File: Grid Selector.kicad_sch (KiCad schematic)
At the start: 74 parts

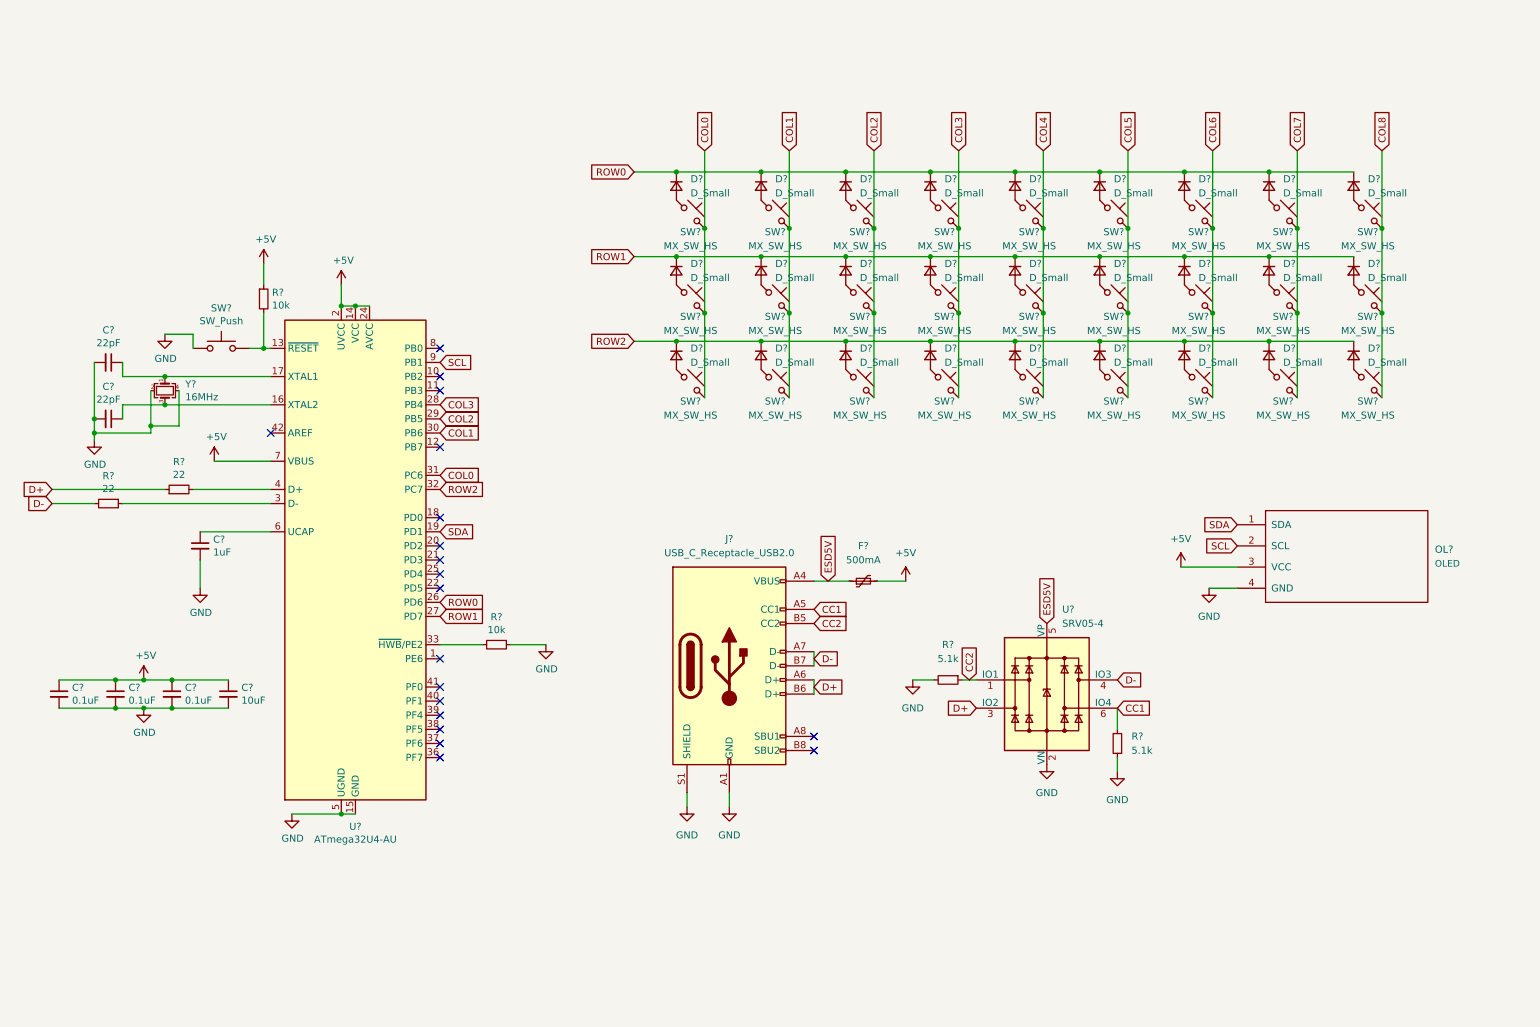
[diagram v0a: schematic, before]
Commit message: added oled library and finished schematics
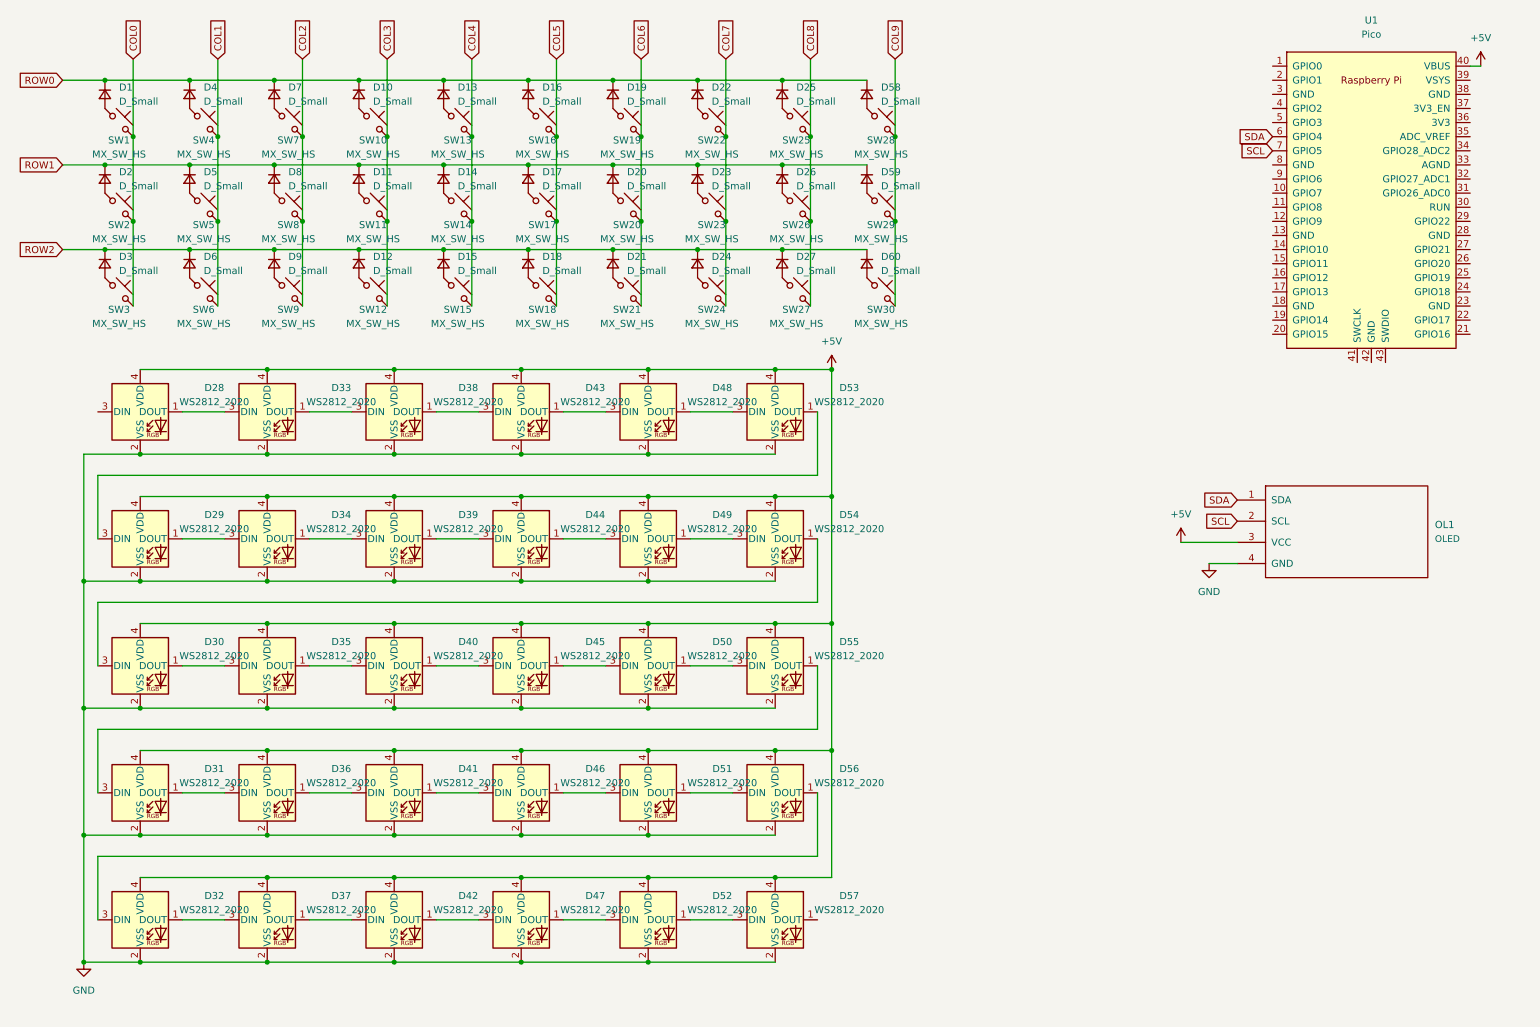
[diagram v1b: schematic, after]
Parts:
- removed C?: 10uF, Capacitor_SMD:C_0805_2012Metric, symbol Device:C_Small
- removed C? (x3): 0.1uF, Capacitor_SMD:C_0805_2012Metric, symbol Device:C_Small
- removed C? (x2): 22pF, Capacitor_SMD:C_0805_2012Metric, symbol Device:C_Small
- removed C?: 1uF, Capacitor_SMD:C_0805_2012Metric, symbol Device:C_Small
- removed F?: 500mA, Fuse:Fuse_1206_3216Metric, symbol Device:Polyfuse_Small
- removed J?: USB_C_Receptacle_USB2.0, Connector_USB:USB_C_Receptacle_HRO_TYPE-C-31-M-12, symbol Connector:USB_C_Receptacle_USB2.0
- removed OL?: OLED, kbd:OLED_v2, symbol kbd:OLED
- removed R? (x2): 5.1k, Resistor_SMD:R_0805_2012Metric, symbol Device:R_Small
- removed R? (x2): 22, Resistor_SMD:R_0805_2012Metric, symbol Device:R_Small
- removed R? (x2): 10k, Resistor_SMD:R_0805_2012Metric, symbol Device:R_Small
- removed SW?: SW_Push, marbastlib-various:SW_SPST_SKQG_WithStem, symbol Switch:SW_Push
- removed U?: ATmega32U4-AU, Package_QFP:TQFP-44_10x10mm_P0.8mm, symbol hayabusa04-rescue:ATmega32U4-AU-MCU_Microchip_ATmega
- removed U?: SRV05-4, Package_TO_SOT_SMD:SOT-23-6, symbol Power_Protection:SRV05-4
- removed Y?: 16MHz, Crystal:Crystal_SMD_3225-4Pin_3.2x2.5mm, symbol Device:Crystal_GND24_Small
- added D28, D29, D30, D31, D32, D33, D34, D35, D36, D37, D38, D39, D40, D41, D42, D43, D44, D45, D46, D47, D48, D49, D50, D51, D52, D53, D54, D55, D56, D57: WS2812_2020, marbastlib-various:LED_WS2812_2020, symbol marbastlib-various:WS2812_2020
- added D58, D59, D60: D_Small, Diode_SMD:D_SOD-123, symbol Device:D_Small
- added OL1: OLED, kbd:OLED_v2, symbol kbd:OLED
- added SW28, SW29, SW30: MX_SW_HS, marbastlib-mx:SW_MX_HS_1u, symbol marbastlib-mx:MX_SW_HS
- added U1: Pico, RPi_Pico:RPi_Pico_SMD_TH, symbol MCU_RaspberryPi_and_Boards:Pico
- gave numbers to parts that had none: 54
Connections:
- net +5V: now also D28.4 (VDD), D29.4 (VDD), D30.4 (VDD), D31.4 (VDD), D32.4 (VDD), D33.4 (VDD), D34.4 (VDD), D35.4 (VDD), D36.4 (VDD), D37.4 (VDD), D38.4 (VDD), D39.4 (VDD), D40.4 (VDD), D41.4 (VDD), D42.4 (VDD), D43.4 (VDD), D44.4 (VDD), D45.4 (VDD), D46.4 (VDD), D47.4 (VDD), D48.4 (VDD), D49.4 (VDD), D50.4 (VDD), D51.4 (VDD), D52.4 (VDD), D53.4 (VDD), D54.4 (VDD), D55.4 (VDD), D56.4 (VDD), D57.4 (VDD), OL1.3 (VCC), U1.40 (VBUS)
- net GND: now also D28.2 (VSS), D29.2 (VSS), D30.2 (VSS), D31.2 (VSS), D32.2 (VSS), D33.2 (VSS), D34.2 (VSS), D35.2 (VSS), D36.2 (VSS), D37.2 (VSS), D38.2 (VSS), D39.2 (VSS), D40.2 (VSS), D41.2 (VSS), D42.2 (VSS), D43.2 (VSS), D44.2 (VSS), D45.2 (VSS), D46.2 (VSS), D47.2 (VSS), D48.2 (VSS), D49.2 (VSS), D50.2 (VSS), D51.2 (VSS), D52.2 (VSS), D53.2 (VSS), D54.2 (VSS), D55.2 (VSS), D56.2 (VSS), D57.2 (VSS), OL1.4 (GND)
- net ROW0: now also D58.1 (K)
- net ROW1: now also D59.1 (K)
- net ROW2: now also D60.1 (K)
- net SCL: now also OL1.2 (SCL), U1.7 (GPIO5)
- net SDA: now also OL1.1 (SDA), U1.6 (GPIO4)
- new net: D40.1 (DOUT), D45.3 (DIN)
- new net: D35.1 (DOUT), D40.3 (DIN)
- new net: D32.3 (DIN), D56.1 (DOUT)
- new net: D51.1 (DOUT), D56.3 (DIN)
- new net: D37.1 (DOUT), D42.3 (DIN)
- new net: D32.1 (DOUT), D37.3 (DIN)
- new net: D58.2 (A), SW28.1
- new net: D42.1 (DOUT), D47.3 (DIN)
- new net: D60.2 (A), SW30.1
- new net: D45.1 (DOUT), D50.3 (DIN)
- new net: D36.1 (DOUT), D41.3 (DIN)
- new net: D31.1 (DOUT), D36.3 (DIN)
- new net: D47.1 (DOUT), D52.3 (DIN)
- new net: D48.1 (DOUT), D53.3 (DIN)
- new net: D43.1 (DOUT), D48.3 (DIN)
- new net: D29.1 (DOUT), D34.3 (DIN)
- new net: D29.3 (DIN), D53.1 (DOUT)
- new net: D59.2 (A), SW29.1
- new net: D31.3 (DIN), D55.1 (DOUT)
- new net: D50.1 (DOUT), D55.3 (DIN)
- new net: D52.1 (DOUT), D57.3 (DIN)
- new net: D33.1 (DOUT), D38.3 (DIN)
- new net: D28.1 (DOUT), D33.3 (DIN)
- new net: D46.1 (DOUT), D51.3 (DIN)
- new net: D30.3 (DIN), D54.1 (DOUT)
- new net: D49.1 (DOUT), D54.3 (DIN)
- new net: D38.1 (DOUT), D43.3 (DIN)
- new net: D44.1 (DOUT), D49.3 (DIN)
- new net: D30.1 (DOUT), D35.3 (DIN)
- new net: D39.1 (DOUT), D44.3 (DIN)
- new net: D41.1 (DOUT), D46.3 (DIN)
- new net: D34.1 (DOUT), D39.3 (DIN)
- new net COL9: SW28.2, SW29.2, SW30.2
- no-connect marks 19 -> 0
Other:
- moved on the sheet: D1, D10, D11, D12, D13, D14, D15, D16, D17, D18, D19, D2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

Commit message: placed switch matrix
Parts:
- U1: footprint RPi_Pico:RPi_Pico_SMD_TH -> MCU_RaspberryPi_and_Boards:RPi_Pico_SMD_TH
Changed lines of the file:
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@@
     (property "Reference" "U1" (id 0) (at 259.715 17.145 0))
     (property "Value" "Pico" (id 1) (at 259.715 19.685 0))
-    (property "Footprint" "RPi_Pico:RPi_Pico_SMD_TH" (id 2) (at 259.715 49.53 90)
+    (property "Footprint" "MCU_RaspberryPi_and_Boards:RPi_Pico_SMD_TH" (id 2) (at 259.715 49.53 90)
       (effects (font (size 1.27 1.27)) hide)
     )
@@
     )
     (path "/3a4de697-ff09-4113-abdb-fad2a038151e"
-      (reference "U1") (unit 1) (value "Pico") (footprint "RPi_Pico:RPi_Pico_SMD_TH")
-    )
-  )
+      (reference "U1") (unit 1) (value "Pico") (footprint "MCU_RaspberryPi_and_Boards:RPi_Pico_SMD_TH")
+    )
+  )

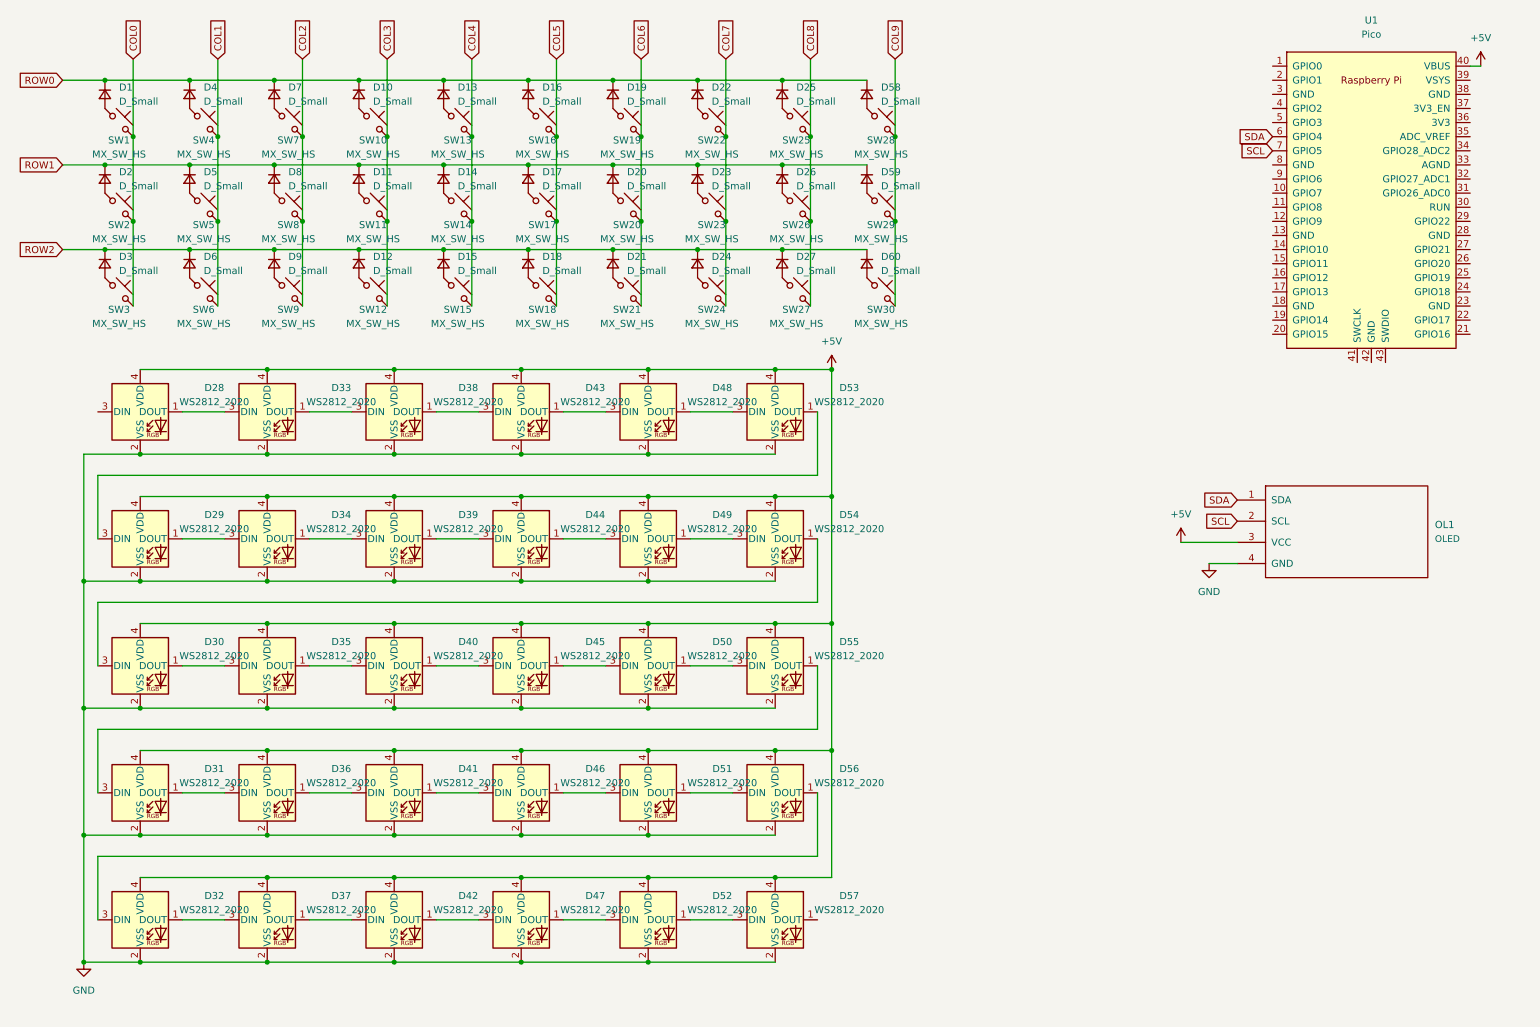
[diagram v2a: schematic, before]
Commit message: updated switch matrix
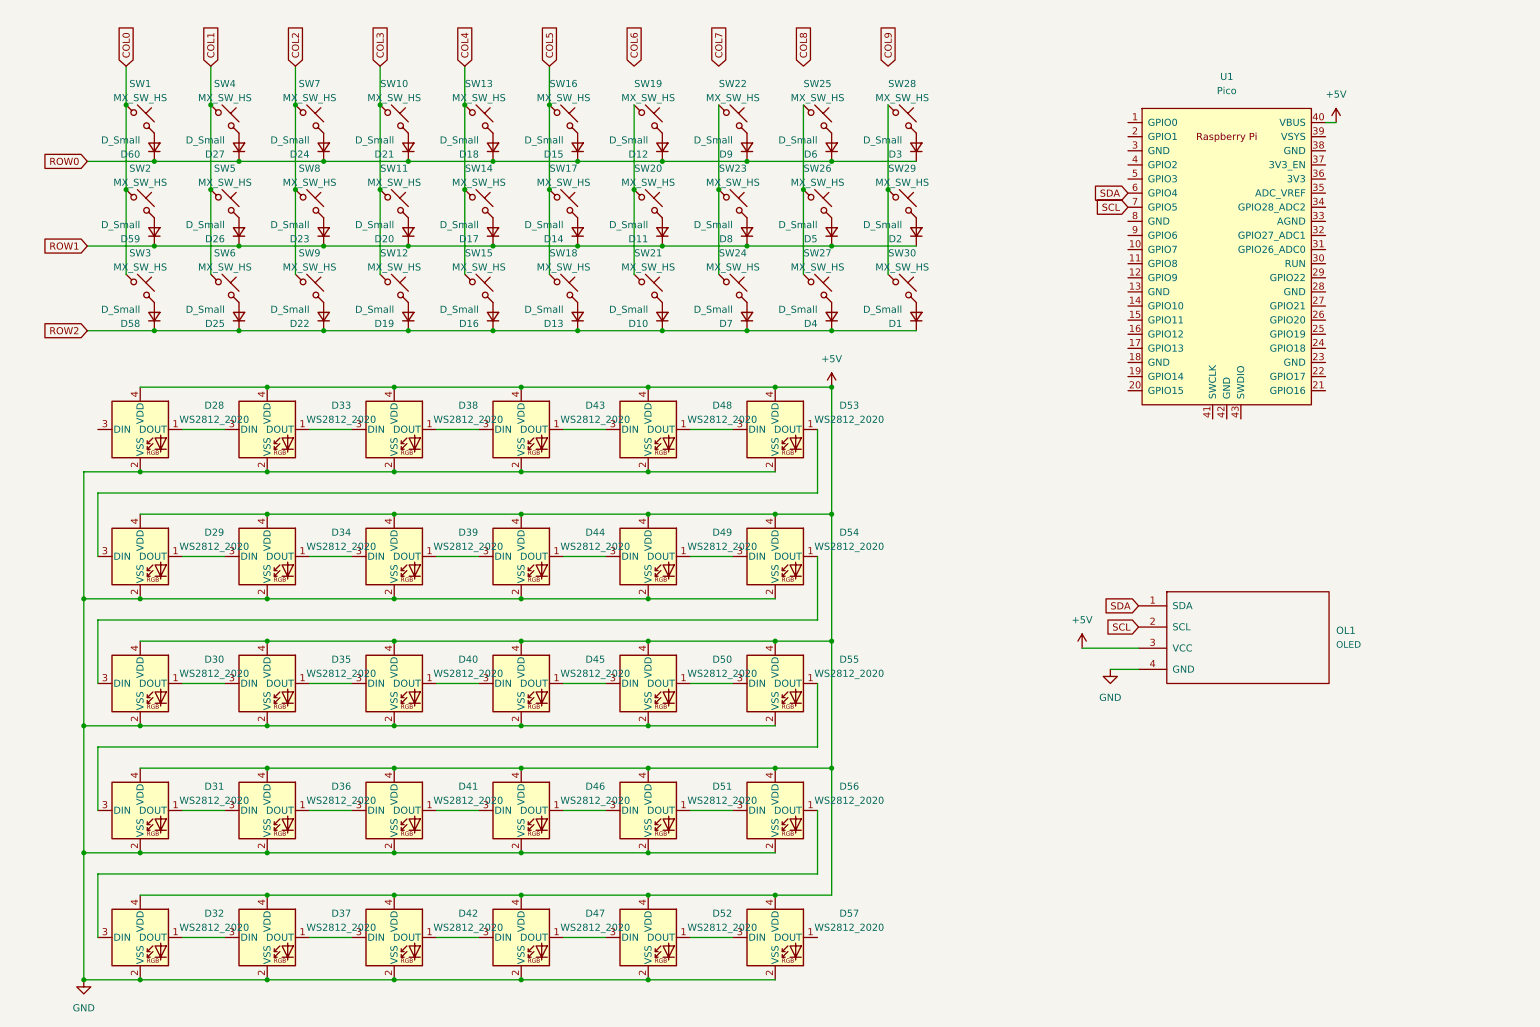
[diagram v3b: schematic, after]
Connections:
- net COL0: now also SW1.1, SW2.1, SW3.1; no longer SW1.2, SW2.2, SW3.2
- net COL1: now also SW4.1, SW5.1, SW6.1; no longer SW4.2, SW5.2, SW6.2
- net COL2: now also SW7.1, SW8.1, SW9.1; no longer SW7.2, SW8.2, SW9.2
- net COL3: now also SW10.1, SW11.1, SW12.1; no longer SW10.2, SW11.2, SW12.2
- net COL4: now also SW13.1, SW14.1, SW15.1; no longer SW13.2, SW14.2, SW15.2
- net COL5: now also SW16.1, SW17.1, SW18.1; no longer SW16.2, SW17.2, SW18.2
- net COL6: no longer SW19.2, SW20.2, SW21.2
- net COL7: no longer SW22.2, SW23.2, SW24.2
- net COL8: no longer SW25.2, SW26.2, SW27.2
- net COL9: no longer SW28.2, SW29.2, SW30.2
- net ROW0: now also D12.1 (K), D15.1 (K), D18.1 (K), D21.1 (K), D24.1 (K), D27.1 (K), D3.1 (K), D6.1 (K), D60.1 (K), D9.1 (K); no longer D1.1 (K), D10.1 (K), D13.1 (K), D16.1 (K), D19.1 (K), D22.1 (K), D25.1 (K), D4.1 (K), D58.1 (K), D7.1 (K)
- net ROW2: now also D1.1 (K), D10.1 (K), D13.1 (K), D16.1 (K), D19.1 (K), D22.1 (K), D25.1 (K), D4.1 (K), D58.1 (K), D7.1 (K); no longer D12.1 (K), D15.1 (K), D18.1 (K), D21.1 (K), D24.1 (K), D27.1 (K), D3.1 (K), D6.1 (K), D60.1 (K), D9.1 (K)
- net at D13.2 (A): now also SW18.2; no longer SW13.1
- net at SW27.1: now also SW25.1, SW26.1; no longer D27.2 (A)
- net at D9.2 (A): now also SW22.2; no longer SW9.1
- net at D8.2 (A): now also SW23.2; no longer SW8.1
- net at D7.2 (A): now also SW24.2; no longer SW7.1
- net at D24.2 (A): now also SW7.2; no longer SW24.1
- net at D10.2 (A): now also SW21.2; no longer SW10.1
- net at D20.2 (A): now also SW11.2; no longer SW20.1
- net at SW19.1: now also SW20.1, SW21.1; no longer D19.2 (A)
- net at D15.2 (A): now also SW16.2; no longer SW15.1
- net at D18.2 (A): now also SW13.2; no longer SW18.1
- net at D17.2 (A): now also SW14.2; no longer SW17.1
- net at D16.2 (A): now also SW15.2; no longer SW16.1
- net at D58.2 (A): now also SW3.2; no longer SW28.1
- net at D26.2 (A): now also SW5.2; no longer SW26.1
- net at D60.2 (A): now also SW1.2; no longer SW30.1
- net at D5.2 (A): now also SW26.2; no longer SW5.1
- net at D4.2 (A): now also SW27.2; no longer SW4.1
- net at SW29.1: now also SW28.1, SW30.1; no longer D59.2 (A)
- net at D11.2 (A): now also SW20.2; no longer SW11.1
- net at D3.2 (A): now also SW28.2; no longer SW3.1
- net at D6.2 (A): now also SW25.2; no longer SW6.1
- net at D25.2 (A): now also SW6.2; no longer SW25.1
- net at D12.2 (A): now also SW19.2; no longer SW12.1
- net at D21.2 (A): now also SW10.2; no longer SW21.1
- net at D23.2 (A): now also SW8.2; no longer SW23.1
- net at D1.2 (A): now also SW30.2; no longer SW1.1
- net at D2.2 (A): now also SW29.2; no longer SW2.1
- net at D22.2 (A): now also SW9.2; no longer SW22.1
- net at D14.2 (A): now also SW17.2; no longer SW14.1
- new net: D19.2 (A), SW12.2
- new net: D59.2 (A), SW2.2
- new net: D27.2 (A), SW4.2
- new net: SW22.1, SW23.1, SW24.1
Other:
- moved on the sheet: D1, D10, D11, D12, D13, D14, D15, D16, D17, D18, D19, D2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
